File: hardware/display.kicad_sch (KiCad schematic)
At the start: 0 parts

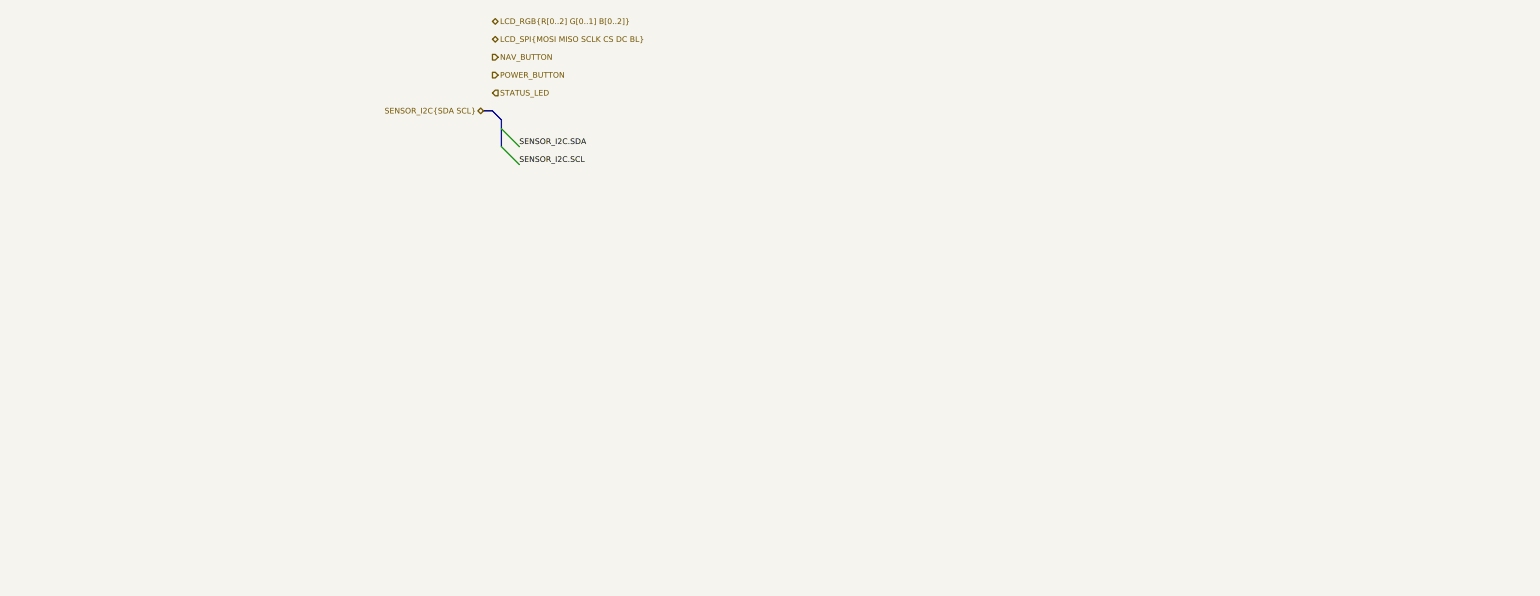
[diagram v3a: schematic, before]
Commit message: changing sdmmc to spi to support lcd rgb mode
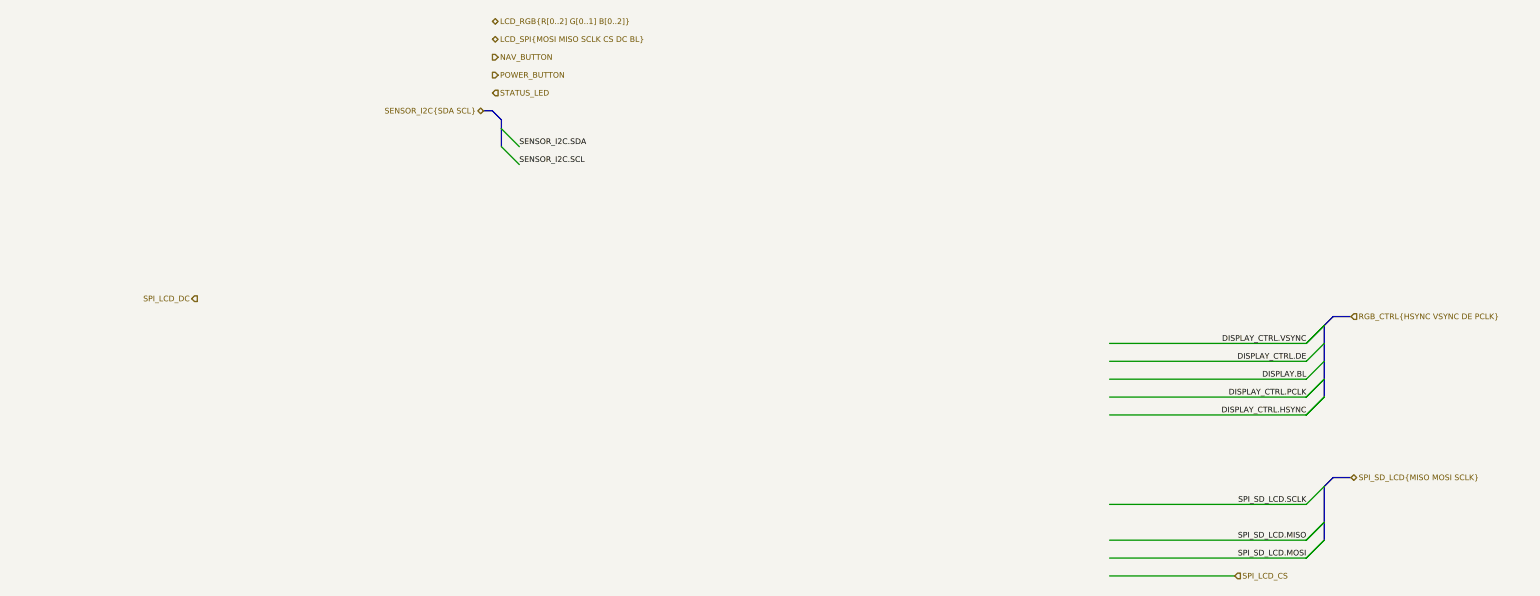
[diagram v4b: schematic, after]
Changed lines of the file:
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@@
     (company "Frisius")
+  )
+  (bus_entry (at 210.82 119.38) (size 2.54 -2.54)
+    (stroke (width 0) (type default) (color 0 0 0 0))
   )
   (bus_entry (at 96.52 88.9) (size 2.54 2.54)
     (stroke (width 0) (type default) (color 0 0 0 0))
   )
+  (bus_entry (at 213.36 124.46) (size -2.54 2.54)
+    (stroke (width 0) (type default) (color 0 0 0 0))
+  )
+  (bus_entry (at 213.36 147.32) (size -2.54 2.54)
+    (stroke (width 0) (type default) (color 0 0 0 0))
+  )
   (bus_entry (at 96.52 91.44) (size 2.54 2.54)
+    (stroke (width 0) (type default) (color 0 0 0 0))
+  )
+  (bus_entry (at 213.36 144.78) (size -2.54 2.54)
+    (stroke (width 0) (type default) (color 0 0 0 0))
+  )
+  (bus_entry (at 210.82 129.54) (size 2.54 -2.54)
+    (stroke (width 0) (type default) (color 0 0 0 0))
+  )
+  (bus_entry (at 213.36 139.7) (size -2.54 2.54)
+    (stroke (width 0) (type default) (color 0 0 0 0))
+  )
+  (bus_entry (at 213.36 127) (size -2.54 2.54)
+    (stroke (width 0) (type default) (color 0 0 0 0))
+  )
+  (bus_entry (at 213.36 116.84) (size -2.54 2.54)
+    (stroke (width 0) (type default) (color 0 0 0 0))
+  )
+  (bus_entry (at 210.82 149.86) (size 2.54 -2.54)
+    (stroke (width 0) (type default) (color 0 0 0 0))
+  )
+  (bus_entry (at 210.82 127) (size 2.54 -2.54)
+    (stroke (width 0) (type default) (color 0 0 0 0))
+  )
+  (bus_entry (at 210.82 121.92) (size 2.54 -2.54)
+    (stroke (width 0) (type default) (color 0 0 0 0))
+  )
+  (bus_entry (at 210.82 124.46) (size 2.54 -2.54)
+    (stroke (width 0) (type default) (color 0 0 0 0))
+  )
+  (bus_entry (at 213.36 144.78) (size -2.54 2.54)
     (stroke (width 0) (type default) (color 0 0 0 0))
   )
@@
     (stroke (width 0) (type default) (color 0 0 0 0))
   )
+  (wire (pts (xy 182.88 127) (xy 210.82 127))
+    (stroke (width 0) (type default) (color 0 0 0 0))
+  )
+  (bus (pts (xy 213.36 119.38) (xy 213.36 121.92))
+    (stroke (width 0) (type default) (color 0 0 0 0))
+  )
+  (wire (pts (xy 182.88 121.92) (xy 210.82 121.92))
+    (stroke (width 0) (type default) (color 0 0 0 0))
+  )
   (bus (pts (xy 96.52 87.63) (xy 96.52 88.9))
     (stroke (width 0) (type default) (color 0 0 0 0))
+  )
+  (bus (pts (xy 214.63 138.43) (xy 217.17 138.43))
+    (stroke (width 0) (type default) (color 0 0 0 0))
+  )
+  (bus (pts (xy 213.36 121.92) (xy 213.36 124.46))
+    (stroke (width 0) (type default) (color 0 0 0 0))
+  )
+  (bus (pts (xy 213.36 139.7) (xy 214.63 138.43))
+    (stroke (width 0) (type default) (color 0 0 0 0))
+  )
+  (bus (pts (xy 213.36 124.46) (xy 213.36 127))
+    (stroke (width 0) (type default) (color 0 0 0 0))
+  )
+  (wire (pts (xy 182.88 142.24) (xy 210.82 142.24))
+    (stroke (width 0) (type default) (color 0 0 0 0))
+  )
+  (wire (pts (xy 182.88 149.86) (xy 210.82 149.86))
+    (stroke (width 0) (type default) (color 0 0 0 0))
+  )
+  (bus (pts (xy 217.17 115.57) (xy 214.63 115.57))
+    (stroke (width 0) (type default) (color 0 0 0 0))
+  )
+  (bus (pts (xy 213.36 119.38) (xy 213.36 116.84))
+    (stroke (width 0) (type default) (color 0 0 0 0))
+  )
+  (bus (pts (xy 214.63 115.57) (xy 213.36 116.84))
+    (stroke (width 0) (type default) (color 0 0 0 0))
+  )
+  (bus (pts (xy 213.36 139.7) (xy 213.36 144.78))
+    (stroke (width 0) (type default) (color 0 0 0 0))
+  )
+  (wire (pts (xy 182.88 119.38) (xy 210.82 119.38))
+    (stroke (width 0) (type default) (color 0 0 0 0))
+  )
+  (wire (pts (xy 182.88 129.54) (xy 210.82 129.54))
+    (stroke (width 0) (type default) (color 0 0 0 0))
+  )
+  (wire (pts (xy 182.88 152.4) (xy 200.66 152.4))
+    (stroke (width 0) (type default) (color 0 0 0 0))
+  )
+  (wire (pts (xy 182.88 147.32) (xy 210.82 147.32))
+    (stroke (width 0) (type default) (color 0 0 0 0))
+  )
+  (bus (pts (xy 213.36 144.78) (xy 213.36 147.32))
+    (stroke (width 0) (type default) (color 0 0 0 0))
+  )
+  (wire (pts (xy 182.88 124.46) (xy 210.82 124.46))
+    (stroke (width 0) (type default) (color 0 0 0 0))
+  )
+  (label "SPI_SD_LCD.MISO" (at 210.82 147.32 180)
+    (effects (font (size 0.8 0.8)) (justify right bottom))
+  )
+  (label "SPI_SD_LCD.SCLK" (at 210.82 142.24 180)
+    (effects (font (size 0.8 0.8)) (justify right bottom))
   )
   (label "SENSOR_I2C.SDA" (at 99.06 91.44 0)
     (effects (font (size 0.8 0.8)) (justify left bottom))
   )
+  (label "DISPLAY_CTRL.DE" (at 210.82 121.92 180)
+    (effects (font (size 0.8 0.8)) (justify right bottom))
+  )
+  (label "DISPLAY_CTRL.HSYNC" (at 210.82 129.54 180)
+    (effects (font (size 0.8 0.8)) (justify right bottom))
+  )
+  (label "DISPLAY_CTRL.PCLK" (at 210.82 127 180)
+    (effects (font (size 0.8 0.8)) (justify right bottom))
+  )
   (label "SENSOR_I2C.SCL" (at 99.06 93.98 0)
     (effects (font (size 0.8 0.8)) (justify left bottom))
+  )
+  (label "DISPLAY_CTRL.VSYNC" (at 210.82 119.38 180)
+    (effects (font (size 0.8 0.8)) (justify right bottom))
+  )
+  (label "SPI_SD_LCD.MOSI" (at 210.82 149.86 180)
+    (effects (font (size 0.8 0.8)) (justify right bottom))
+  )
+  (label "DISPLAY.BL" (at 210.82 124.46 180)
+    (effects (font (size 0.8 0.8)) (justify right bottom))
+  )
+  (hierarchical_label "SPI_SD_LCD{MISO MOSI SCLK}" (shape bidirectional) (at 217.17 138.43 0)
+    (effects (font (size 0.8 0.8)) (justify left))
   )
   (hierarchical_label "SENSOR_I2C{SDA SCL}" (shape bidirectional) (at 93.98 86.36 180)
@@
     (effects (font (size 0.8 0.8)) (justify left))
   )
+  (hierarchical_label "SPI_LCD_CS" (shape input) (at 200.66 152.4 0)
+    (effects (font (size 0.8 0.8)) (justify left))
+  )
+  (hierarchical_label "RGB_CTRL{HSYNC VSYNC DE PCLK}" (shape input) (at 217.17 115.57 0)
+    (effects (font (size 0.8 0.8)) (justify left))
+  )
+  (hierarchical_label "SPI_LCD_DC" (shape output) (at 53.34 113.03 180)
+    (effects (font (size 0.8 0.8)) (justify right))
+  )
   (hierarchical_label "LCD_RGB{R[0..2] G[0..1] B[0..2]}" (shape bidirectional) (at 95.25 73.66 0)

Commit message: layout 0 unconnected
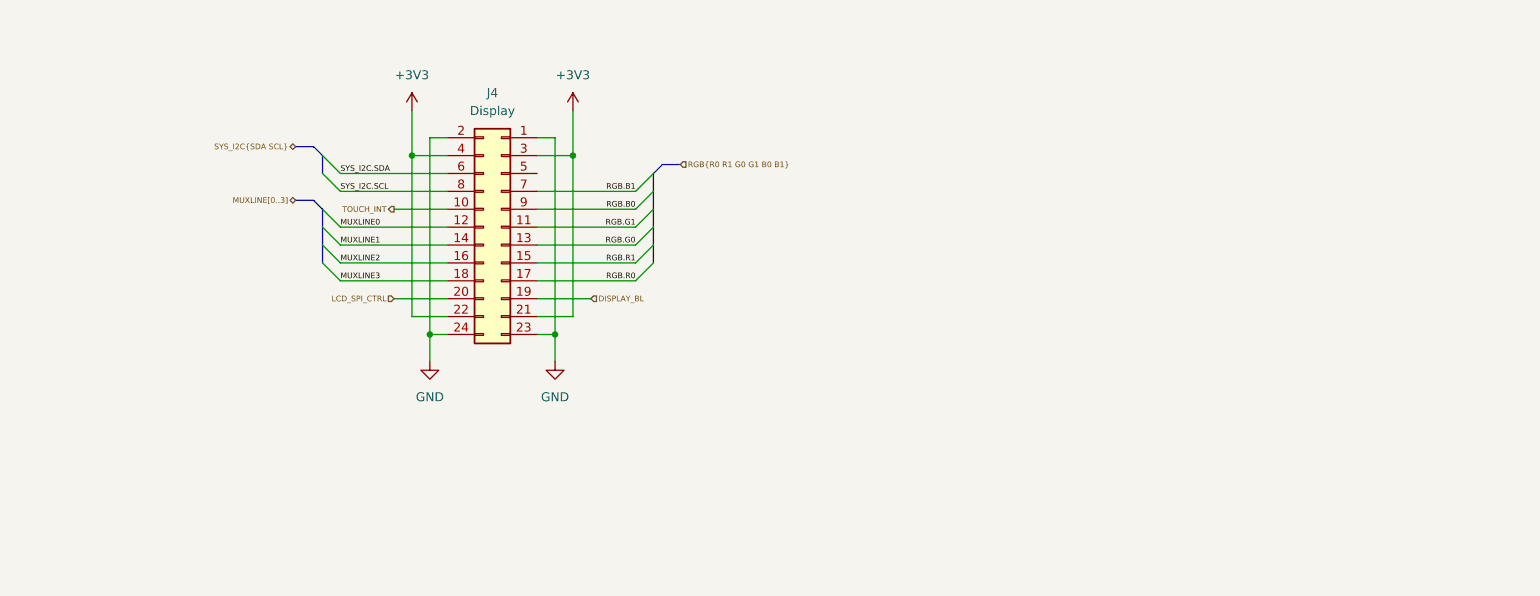
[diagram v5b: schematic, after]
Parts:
- added J4: Display, Connector_Molex:Molex_SlimStack_55560-0241_2x12_P0.50mm_Vertical, symbol Connector_Generic:Conn_02x12_Odd_Even
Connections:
- new net +3V3: J4.21 (Pin_21), J4.22 (Pin_22), J4.3 (Pin_3), J4.4 (Pin_4)
- new net DISPLAY_BL: J4.19 (Pin_19)
- new net GND: J4.1 (Pin_1), J4.2 (Pin_2), J4.23 (Pin_23), J4.24 (Pin_24)
- new net LCD_SPI_CTRL: J4.20 (Pin_20)
- new net MUXLINE0: J4.12 (Pin_12)
- new net MUXLINE1: J4.14 (Pin_14)
- new net MUXLINE2: J4.16 (Pin_16)
- new net MUXLINE3: J4.18 (Pin_18)
- new net RGB.B0: J4.9 (Pin_9)
- new net RGB.B1: J4.7 (Pin_7)
- new net RGB.G0: J4.13 (Pin_13)
- new net RGB.G1: J4.11 (Pin_11)
- new net RGB.R0: J4.17 (Pin_17)
- new net RGB.R1: J4.15 (Pin_15)
- new net SYS_I2C.SCL: J4.8 (Pin_8)
- new net SYS_I2C.SDA: J4.6 (Pin_6)
- new net TOUCH_INT: J4.10 (Pin_10)

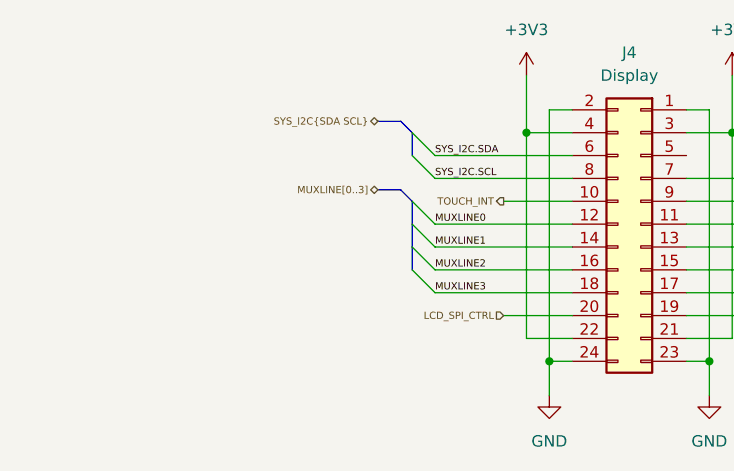
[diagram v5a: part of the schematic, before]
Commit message: merged in lcdboard test work
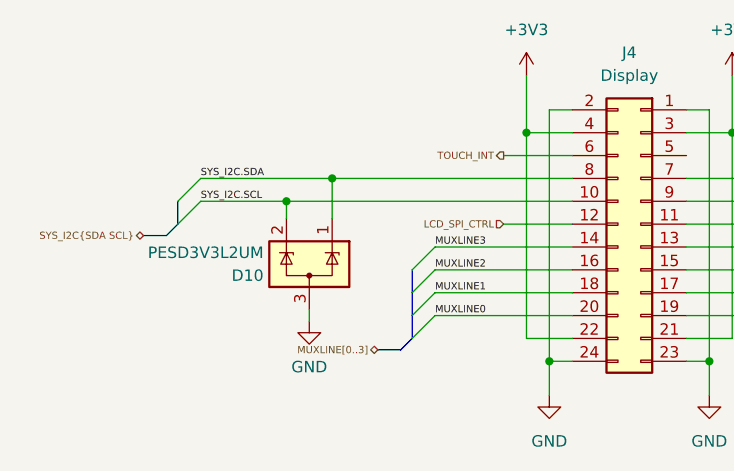
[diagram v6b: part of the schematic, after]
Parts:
- added D10: PESD3V3L2UM, Package_TO_SOT_SMD:SOT-883, symbol Power_Protection:SP0502BAHT
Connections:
- net GND: now also D10.3 (A)
- net LCD_SPI_CTRL: now also J4.12 (Pin_12); no longer J4.20 (Pin_20)
- net MUXLINE0: now also J4.20 (Pin_20); no longer J4.12 (Pin_12)
- net MUXLINE1: now also J4.18 (Pin_18); no longer J4.14 (Pin_14)
- net MUXLINE3: now also J4.14 (Pin_14); no longer J4.18 (Pin_18)
- net SYS_I2C.SCL: now also J4.10 (Pin_10), D10.2 (K); no longer J4.8 (Pin_8)
- net SYS_I2C.SDA: now also J4.8 (Pin_8), D10.1 (K); no longer J4.6 (Pin_6)
- net TOUCH_INT: now also J4.6 (Pin_6); no longer J4.10 (Pin_10)
